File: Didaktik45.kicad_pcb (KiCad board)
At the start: 2 copper layers, 110 parts, among them J1 Conn_01x04_MountingPin, SW1 SW_Push, SW10 SW_Push_45deg, SW11 SW_Push_45deg, SW12 SW_Push_45deg, SW13 SW_Push_45deg, SW14 SW_Push_45deg, SW15 SW_Push_45deg, SW16 SW_Push_45deg, SW17 SW_Push_45deg, SW18 SW_Push_45deg, SW19 SW_Push_45deg, SW2 SW_Push_45deg, SW20 SW_Push_45deg, SW21 SW_Push_45deg, SW22 SW_Push_45deg, SW23 SW_Push_45deg, SW24 SW_Push_45deg, SW25 SW_Push_45deg, SW26 SW_Push_45deg, SW27 SW_Push_45deg, SW28 SW_Push_45deg, SW29 SW_Push_45deg, SW3 SW_Push_45deg, SW30 SW_Push_45deg, SW31 SW_Push_45deg, SW32 SW_Push_45deg, SW33 SW_Push_45deg, SW34 SW_Push_45deg, SW35 SW_Push_45deg, SW36 SW_Push_45deg, SW37 SW_Push_45deg, SW38 SW_Push_45deg, SW39 SW_Push_45deg, SW4 SW_Push_45deg, SW40 SW_Push_45deg, SW41 SW_Push_45deg, SW42 SW_Push_45deg, SW43 SW_Push_45deg, SW44 SW_Push_45deg, SW45 SW_Push_45deg, SW46 SW_Push_45deg, SW5 SW_Push_45deg, SW6 SW_Push_45deg, SW7 SW_Push_45deg, SW8 SW_Push_45deg, SW9 SW_Push_45deg, U1 ATmega32U4-M, Y1 Crystal_GND24_Small

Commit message: D45 & D40 pcbs created & cleaned. D45 plate created
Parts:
- added G***: LOGO, LOGO, F.Cu at (149.2, 65.1)
- added G***: LOGO, LOGO, F.Cu at (149.2, 87.3)
- C1, C2, C3, C4, C5, C6, C7, C8, D1, D10, D11, D12, D13, D14, D15, D16, D17, D18, D19, D2, D20, D21, D22, D23, D24, D25, D26, D27, D28, D29, D3, D30, D31, D32, D33, D34, D35, D36, D37, D38, D39, D4, D40, D41, D43, D44, D45, D46, D47, D5, D6, D7, D8, D9, F1, J1, R1, R2, R3, R4, R5, SW1, U1, Y1: moved to B.Cu
- moved D46 250.1 mm to (277.5, 45.9), turned to 180 degrees
- moved D44 224.8 mm to (258.4, 84.0), turned to 180 degrees
- moved Y1 223.2 mm to (29.7, 81.2), turned to 45 degrees
- moved R2 220.9 mm to (24.3, 69.8), turned to -90 degrees
- moved C7 216.1 mm to (29.1, 75.4), turned to 135 degrees
- moved SW43 212.6 mm to (258.4, 77.7)
- moved D1 203.2 mm to (20.3, 45.9), turned to 180 degrees
- moved C8 199.3 mm to (26.4, 70.5), turned to 90 degrees
- moved D6 197.6 mm to (48.9, 66.5), turned to 180 degrees
- moved R3 197.0 mm to (28.2, 76.3), turned to 135 degrees
- moved C6 187.7 mm to (25.1, 73.6), turned to 45 degrees
- moved C1 187.5 mm to (20.7, 70.5), turned to 90 degrees
- moved D41 184.2 mm to (206.1, 104.6), turned to 180 degrees
- moved D9 182.9 mm to (58.4, 45.9), turned to 180 degrees
- moved D3 181.2 mm to (39.4, 84.0), turned to 180 degrees
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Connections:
- SW43 pad 1: COL6 -> COL5
- SW44 pad 1: COL6 -> COL5
- SW45 pad 1: COL7 -> COL6
- SW46 pad 1: COL7 -> COL6
- U1 pad 10: unconnected-(U1-Pad10) -> LED Power
- U1 pad 18: unconnected-(U1-Pad18) -> ROW5
- U1 pad 19: unconnected-(U1-Pad19) -> ROW4
- U1 pad 20: unconnected-(U1-Pad20) -> COL5
- U1 pad 21: unconnected-(U1-Pad21) -> COL6
- U1 pad 29: unconnected-(U1-Pad29) -> ROW7
- U1 pad 30: unconnected-(U1-Pad30) -> ROW6
- U1 pad 31: unconnected-(U1-Pad31) -> COL4
- U1 pad 36: unconnected-(U1-Pad36) -> COL3
- U1 pad 37: unconnected-(U1-Pad37) -> COL2
- U1 pad 38: unconnected-(U1-Pad38) -> COL1
- U1 pad 39: unconnected-(U1-Pad39) -> COL0
- U1 pad 40: unconnected-(U1-Pad40) -> ROW1
- U1 pad 41: unconnected-(U1-Pad41) -> ROW0
- U1 pad 8: unconnected-(U1-Pad8) -> ROW2
- U1 pad 9: unconnected-(U1-Pad9) -> ROW3
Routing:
- net ROW0: track 0.00 -> 551.8 mm, vias 0 -> 10
- net ROW6: track 0.00 -> 550.9 mm, vias 0 -> 4
- net ROW7: track 0.00 -> 483.1 mm
- net ROW4: track 0.00 -> 469.2 mm, vias 0 -> 2
- net COL4: track 0.00 -> 390.7 mm, vias 0 -> 1
- net ROW2: track 0.00 -> 362.0 mm, vias 0 -> 2
- net ROW1: track 0.00 -> 356.6 mm
- net COL6: track 0.00 -> 350.7 mm, vias 0 -> 1
- net ROW5: track 0.00 -> 350.0 mm
- net COL3: track 0.00 -> 346.0 mm, vias 0 -> 1
- net ROW3: track 0.00 -> 340.1 mm
- net COL5: track 0.00 -> 334.2 mm, vias 0 -> 1
- net COL2: track 0.00 -> 304.1 mm, vias 0 -> 1
- net +5V: track 0.00 -> 284.8 mm, vias 0 -> 5
- net COL1: track 0.00 -> 263.6 mm, vias 0 -> 1
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- added copper zone on B.Cu, net (none)
- added copper zone on F.Cu, net (none)
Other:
- board outline added: 279.4 x 79.4 mm
- board text added: "Didaktik 40"
- board text added: "Didaktik 45 v1.0 by Calvin#0563"

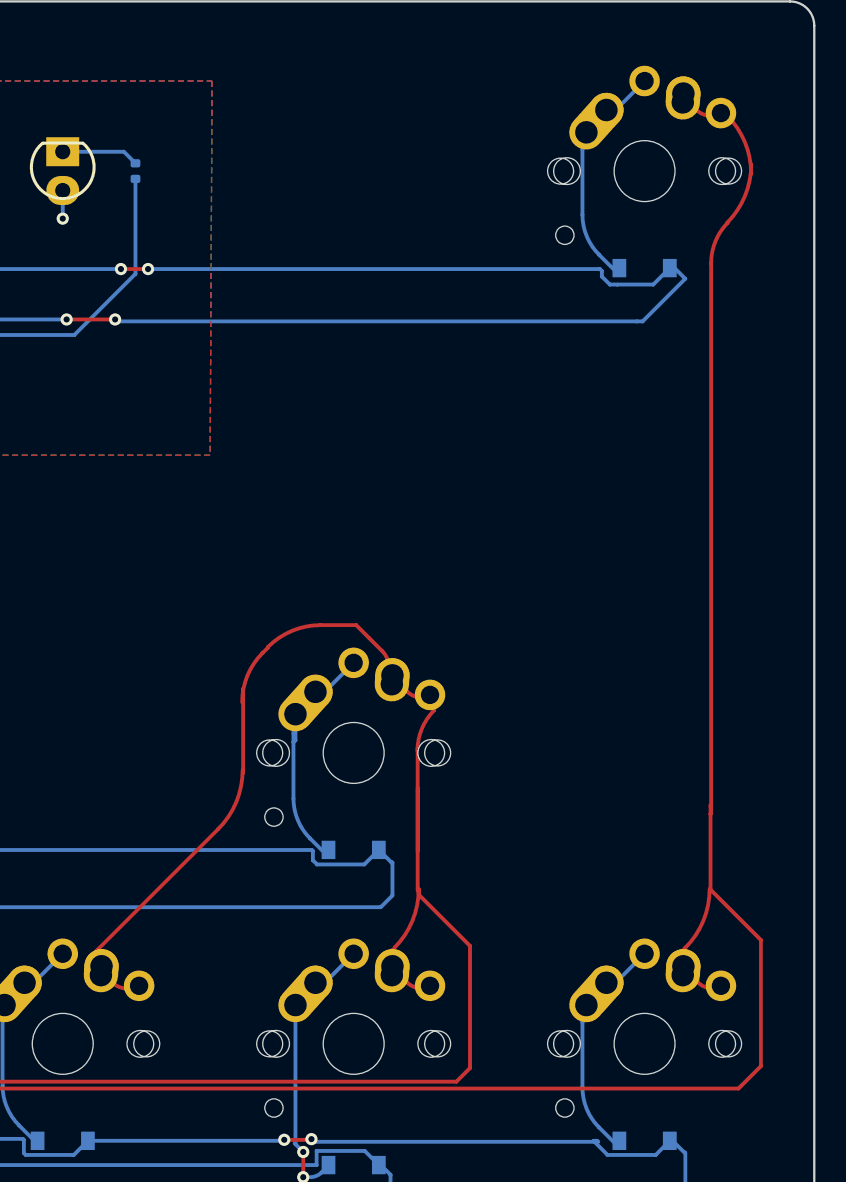
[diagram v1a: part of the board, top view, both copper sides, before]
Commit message: slight alterations to routes
changing rounded for sharp ones
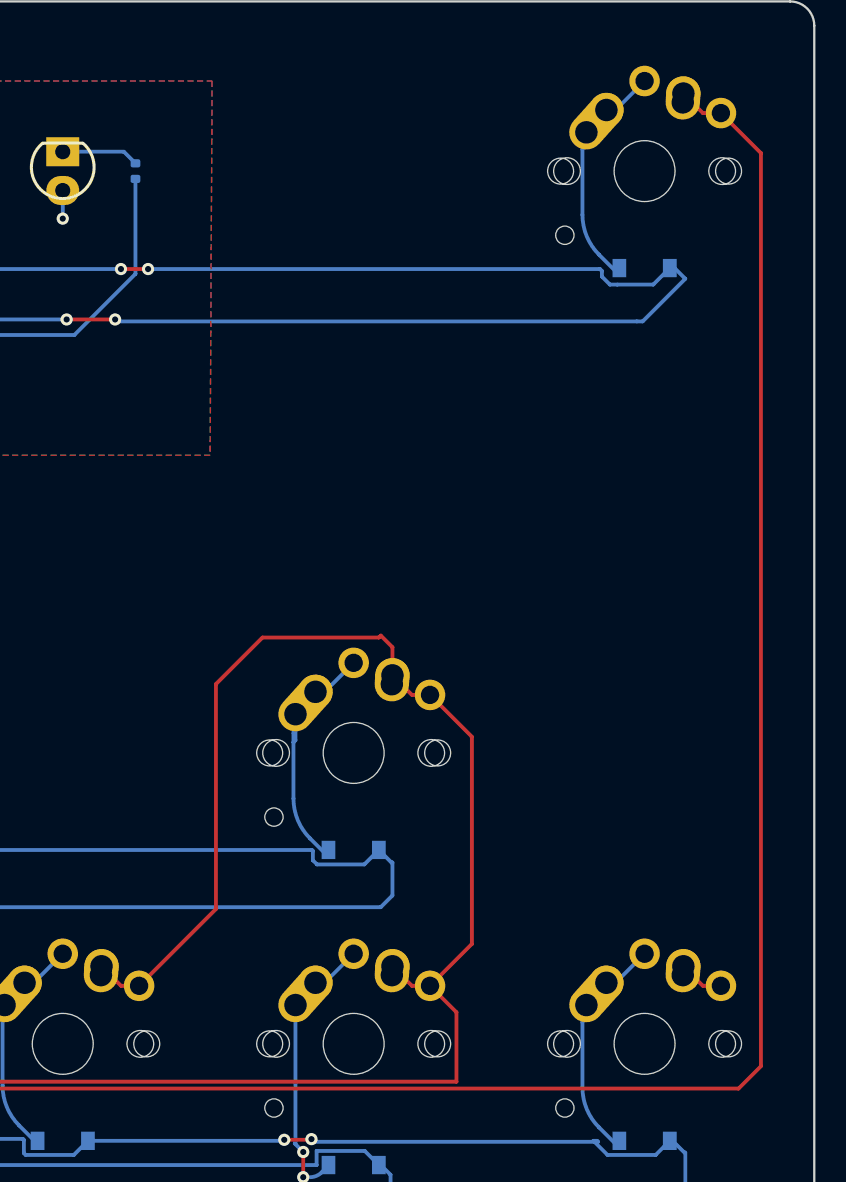
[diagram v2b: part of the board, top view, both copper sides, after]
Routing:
- net COL5: track 334.2 -> 324.4 mm
- net COL6: track 350.7 -> 341.8 mm

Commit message: added multi layout proto
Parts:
- added J2: AVR-ISP-6, random-keyboard-parts:Reset_Pretty-Mask, B.Cu at (36.5, 95.2)
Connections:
- net Net-(R3-Pad2) renamed RESET
- U1 pad 20: COL5 -> MISO
- U1 pad 21: COL6 -> SCK
- U1 pad 22: unconnected-(U1-Pad22) -> MOSI
- U1 pad 26: unconnected-(U1-Pad26) -> COL5
- U1 pad 27: unconnected-(U1-Pad27) -> COL6
- U1 pad 8: ROW2 -> ROW3
- U1 pad 9: ROW3 -> ROW2
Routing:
- net SCK: track 0.00 -> 27.1 mm
- net +5V: track 284.8 -> 309.0 mm, vias 5 -> 7
- net MISO: track 0.00 -> 22.7 mm
- net COL6: track 341.8 -> 363.6 mm
- net MOSI: track 0.00 -> 19.1 mm
- net COL5: track 324.4 -> 343.3 mm, vias 1 -> 3
- net COL1: track 263.6 -> 269.5 mm
- net COL4: track 390.7 -> 396.2 mm
- net GND: track 46.9 -> 52.1 mm, vias 12 -> 16
- net COL2: track 304.1 -> 308.3 mm
- net COL3: track 346.0 -> 350.0 mm
- net COL0: track 229.6 -> 232.9 mm
- net Net-(D44-Pad2): track 17.6 -> 15.0 mm
- net ROW3: track 340.1 -> 342.0 mm
- net ROW5: track 350.0 -> 351.8 mm
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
